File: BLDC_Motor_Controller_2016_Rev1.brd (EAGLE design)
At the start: 113.7 x 80 mm, 98 parts, among them Q1 MOSFET-NCHANNELFQP30N06L, Q2 MOSFET-NCHANNELFQP30N06L, Q3 MOSFET-NCHANNELFQP30N06L, Q4 MOSFET-NCHANNELFQP30N06L, Q5 MOSFET-NCHANNELFQP30N06L, Q6 MOSFET-NCHANNELFQP30N06L, Q7 MOSFET-PCHANNEL, Q8 MOSFET-PCHANNEL

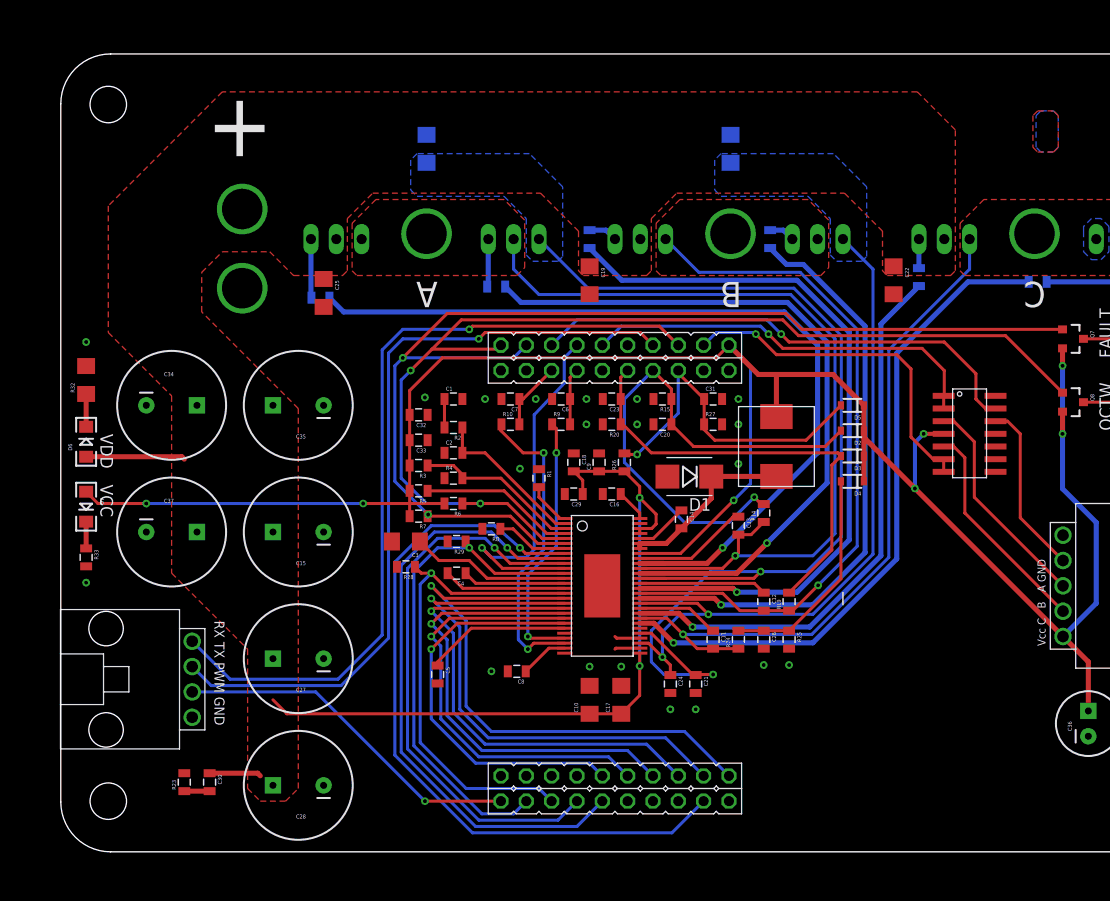
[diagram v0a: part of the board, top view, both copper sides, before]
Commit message: Swapped SL connectors, added APP spacer
Swapped 4-pin Molex SL for two 3-pin SL connectors, added mounting wing
between power inputs, added board description and MRDT logo, moved big
caps around
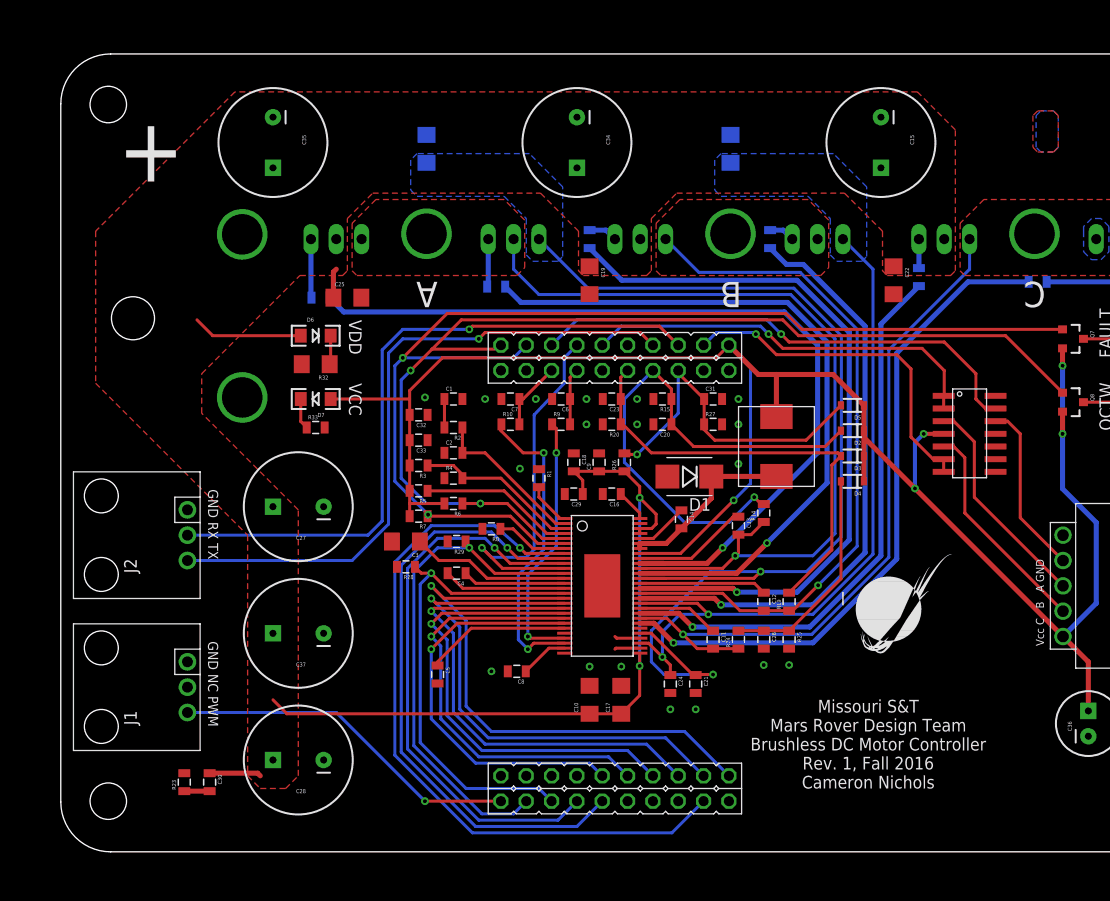
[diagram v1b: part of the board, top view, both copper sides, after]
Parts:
- added J1, J2: SL03THROUGH_HOLE, MRDT-Connectors:MOLEX_SL_03_THROUGH_HOLE
- added U$10: APP_MOUTING_WINGHORIZ, MRDT-Connectors:APP45_MOUNTING_WING_HORIZ
- U$9: value 4PIN -> (none); device Molex-SL:4PIN -> MRDT-Hardware:MRDT_LOGO
- moved C15 70.3 mm to (78.7, 69.8), turned to 270 degrees
- moved U$9 66.5 mm to (76.2, 17.8), turned to 0 degrees
- moved C34 48.4 mm to (48.3, 69.8), turned to 270 degrees
- moved C35 26.5 mm to (17.8, 69.8), turned to 270 degrees
- moved R33 26.4 mm to (22.1, 41.3), turned to 0 degrees
- moved D7 25.4 mm to (22.1, 44.1), turned to 180 degrees
- moved D6 25.4 mm to (22.1, 50.5), turned to 0 degrees
- moved R32 23.1 mm to (22.1, 47.6), turned to 180 degrees
- moved C37 16.3 mm to (20.3, 20.6), turned to 180 degrees
- moved C27 15.2 mm to (20.3, 33.3)
- moved U$4 11.0 mm to (-13.5, 40.3)
- moved C28 2.54 mm to (20.3, 7.94)
- moved U$3 2.54 mm to (-13.5, 56.7)
- moved C25 2.43 mm to (25.2, 54.3), turned to 0 degrees
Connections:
- new net N$36: J1.2
- net GND: now also J1.1, J2.1; no longer U$9.4
- net RX: now also J2.2; no longer U$9.1
- net SPEED_IN: now also J1.3; no longer U$9.3
- net TX: now also J2.3; no longer U$9.2
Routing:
- net VCC: track 218.8 -> 193.8 mm, vias 7 -> 5
- net RX: track 82.5 -> 68.7 mm
- net TX: track 78.9 -> 66.7 mm
- net PVDD: track 91.1 -> 95.2 mm
- net GND: vias 22 -> 20
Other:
- board text added: "GND NC PWM"
- board text added: "GND RX TX"
- board text added: "Missouri S&T Mars Rover Design Team Brushless DC Motor Controller Rev. 1, Fall 2016 Cameron Nichols"
- board text removed: "RX TX PWM GND"

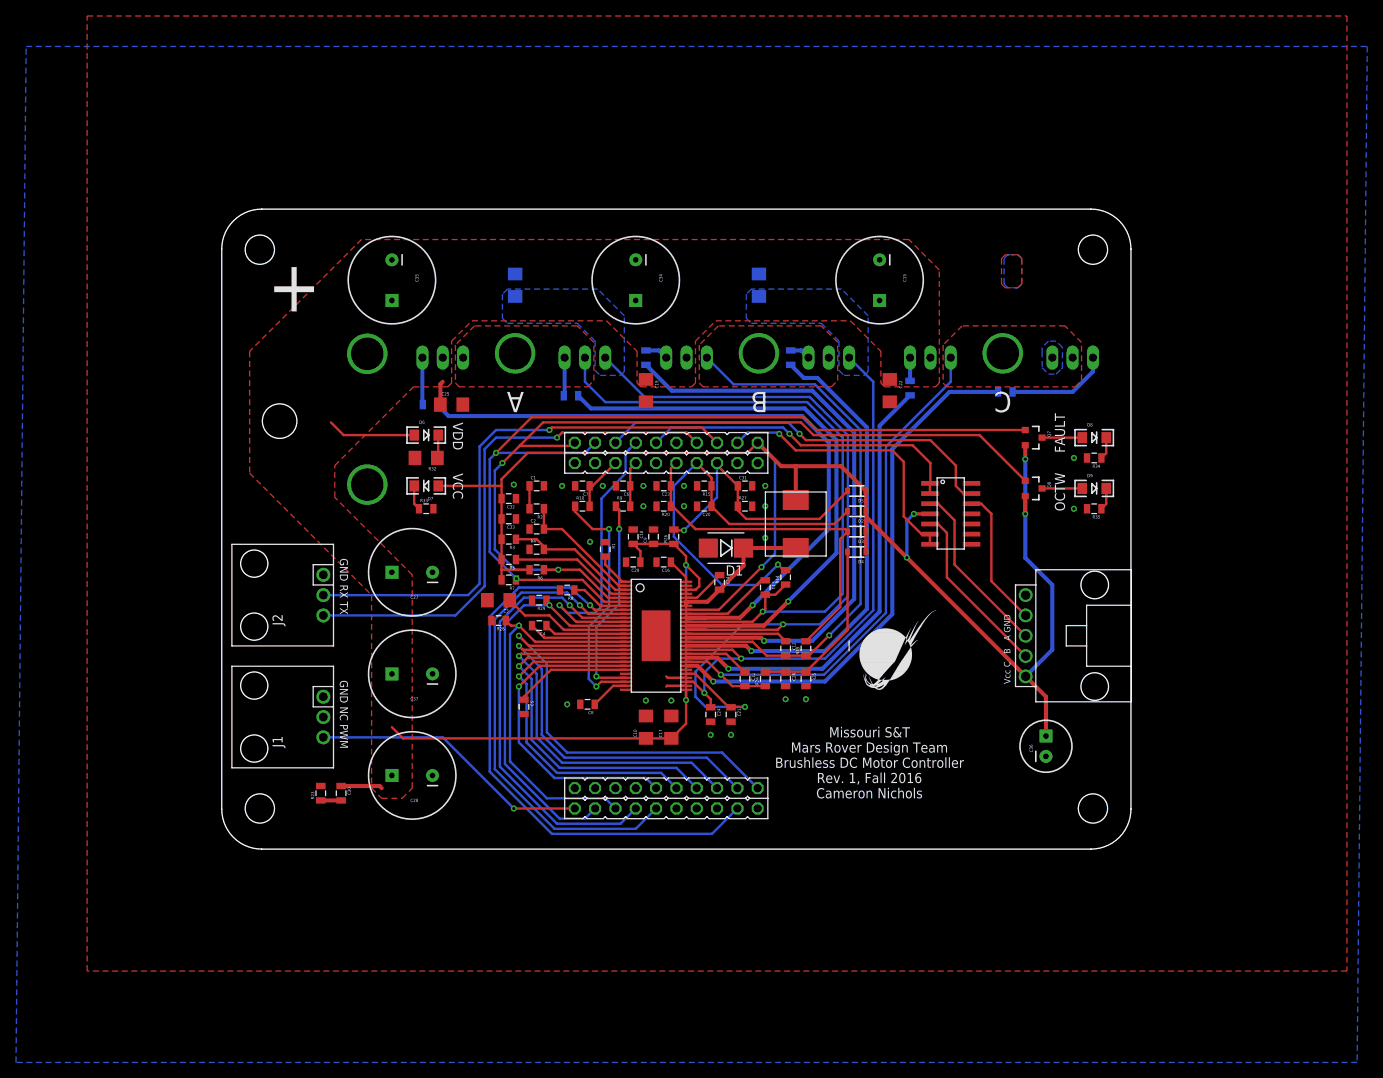
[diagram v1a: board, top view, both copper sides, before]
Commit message: Swapped side-by-side anderson input with stacked orientation
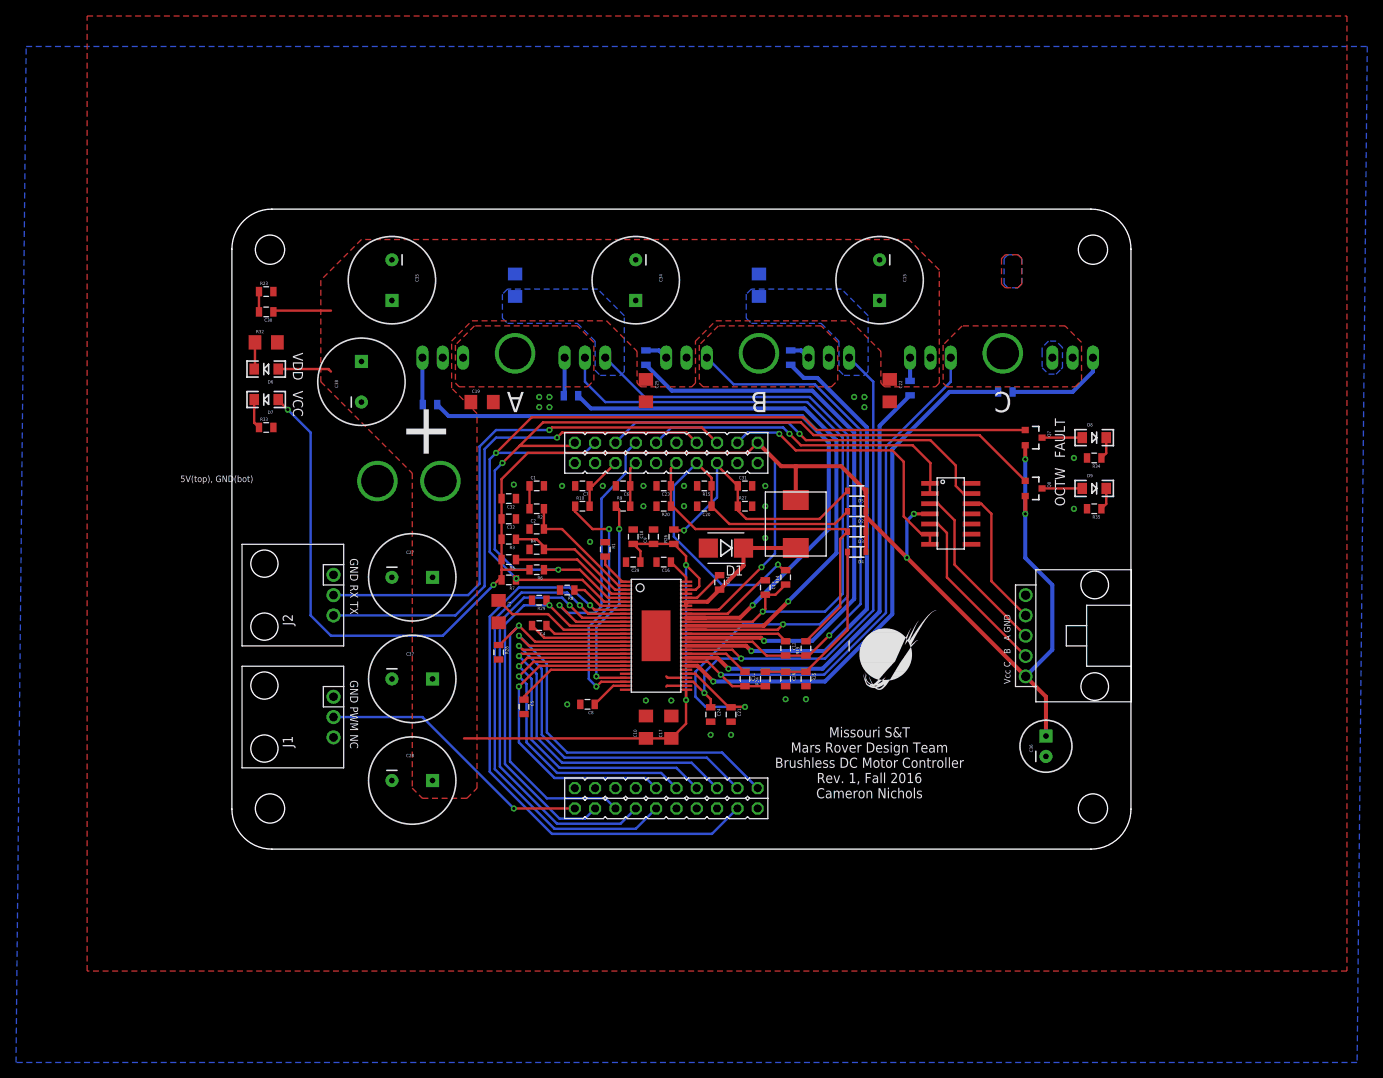
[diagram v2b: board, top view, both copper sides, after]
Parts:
- removed U$10: APP_MOUTING_WINGHORIZ, MRDT-Connectors:APP45_MOUNTING_WING_HORIZ
- removed U$3, U$4: APPPP45_PCB_HORIZ_RIGHT, MRDT-Connectors:APP45_PCB_HORIZ_RIGHT
- added C38: 220u, SparkFun-Passives:CPOL-RADIAL-1000UF-25V
- added J3: APP_2POS_CONFIG5V_HORIZ, MRDT-Connectors:APP45_5V_HORIZ_CONFIG
- J1: value SL03THROUGH_HOLE -> SERVOMOLEX_SL_THRU_HOLE
- moved R23 63.1 mm to (2.06, 68.4), turned to 0 degrees
- moved C30 60.9 mm to (2.06, 65.9), turned to 180 degrees
- moved R32 24.7 mm to (2.06, 62.1), turned to 0 degrees
- moved C25 24.4 mm to (49.5, 56.0), turned to 270 degrees
- moved D7 22.7 mm to (2.06, 54.9)
- moved R33 22.4 mm to (2.06, 51.4)
- moved D6 21.6 mm to (2.06, 58.7), turned to 180 degrees
- moved C19 20.5 mm to (29.1, 54.6), turned to 0 degrees
- moved R28 3.97 mm to (31.1, 23.3), turned to 270 degrees
- moved C3 1.43 mm to (31.1, 28.4), turned to 270 degrees
- moved J1 1.27 mm to (10.5, 15.2)
- moved J2 1.27 mm to (10.5, 30.5)
- moved C28 0.63 mm to (20.3, 7.30), turned to 0 degrees
- moved C27 0.63 mm to (20.3, 32.7), turned to 0 degrees
- moved C37 0.63 mm to (20.3, 20.0), turned to 0 degrees
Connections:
- removed net N$36: J1.2
- net GND: now also C38.2, J3.GND; no longer U$4.P$1
- net PVDD: now also C38.1, J3.5V; no longer U$3.P$1
- net SPEED_IN: now also J1.2; no longer J1.3
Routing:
- net VCC: track 193.8 -> 242.5 mm, vias 5 -> 7
- net PVDD: track 95.2 -> 80.3 mm
- net EN_GATE: track 49.2 -> 50.8 mm
- net N$8: track 16.1 -> 17.5 mm
- net TX: track 66.7 -> 65.4 mm
- net RX: track 68.7 -> 67.5 mm
- net N$24: track 3.11 -> 3.74 mm
- net GND: vias 20 -> 27
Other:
- board size 113.7 x 80 mm -> 112.4 x 80 mm
- board text added: "GND PWM NC"
- board text removed: "GND NC PWM"

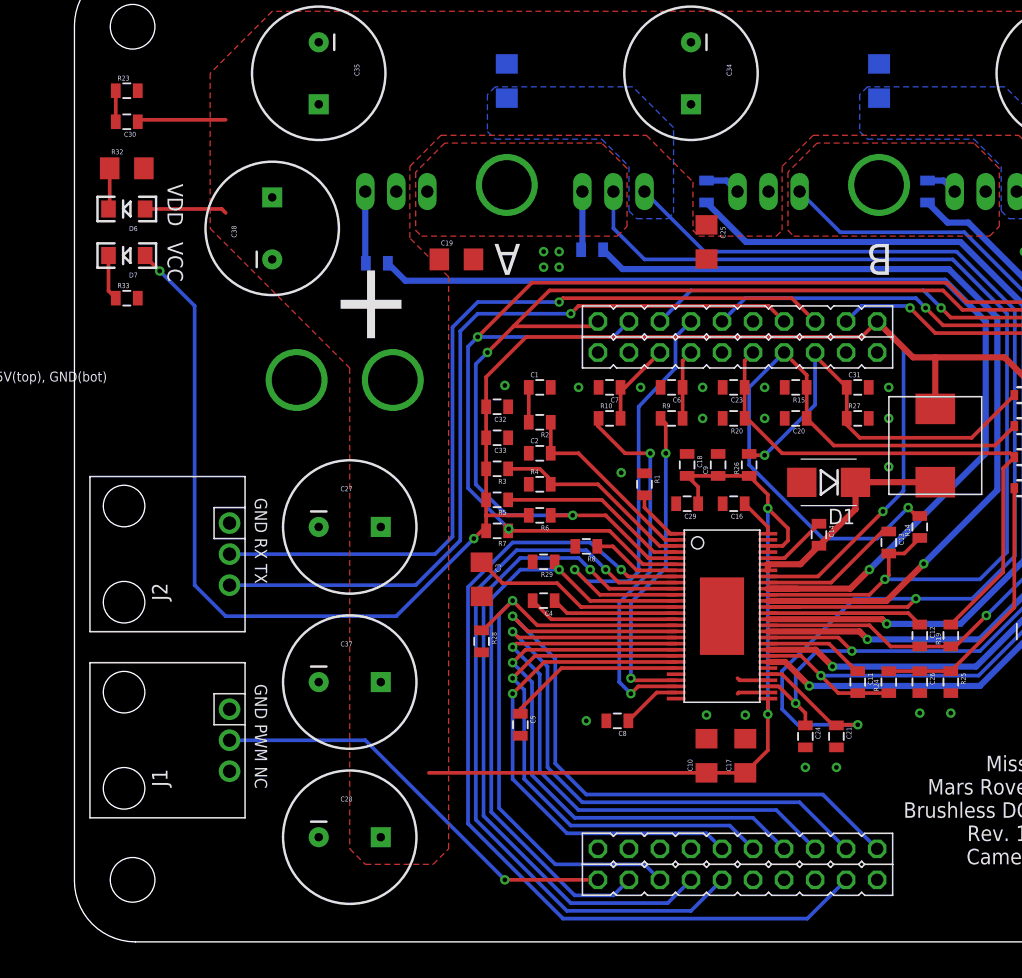
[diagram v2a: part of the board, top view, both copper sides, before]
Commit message: Added RS-485 IC to replace UART
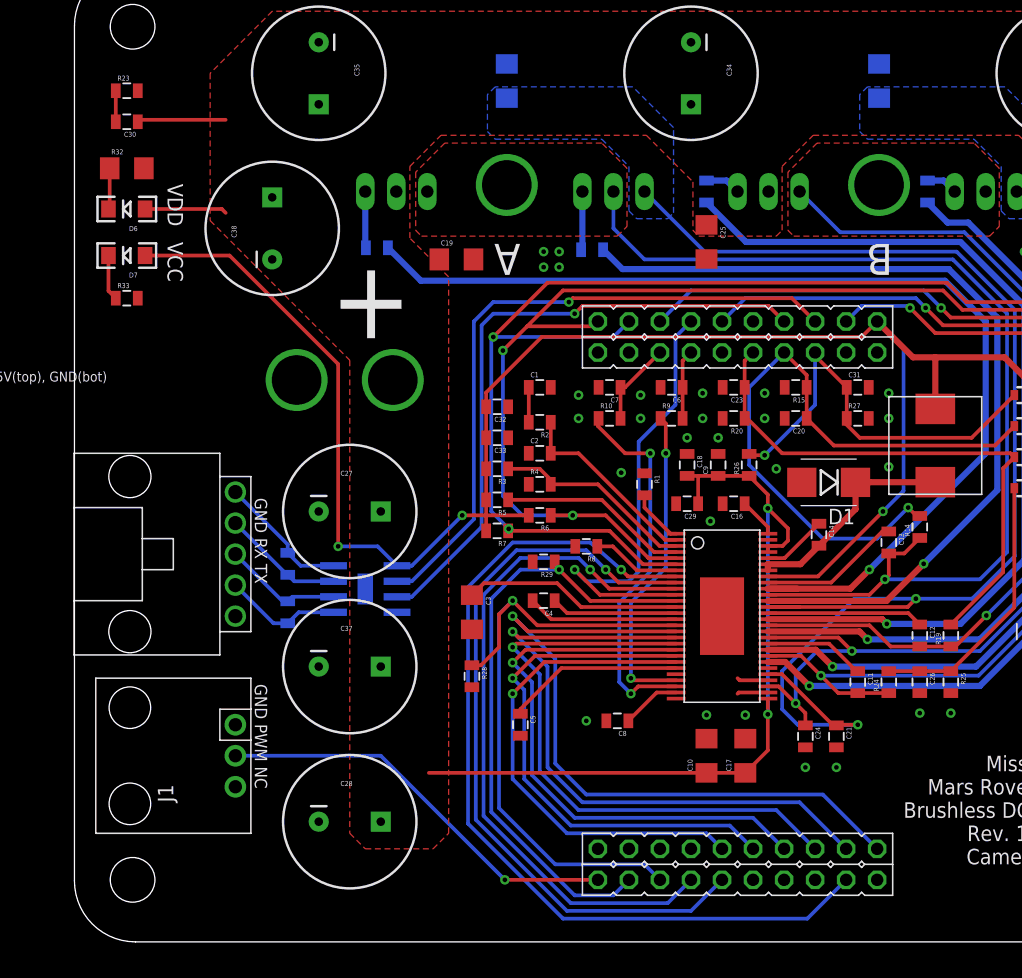
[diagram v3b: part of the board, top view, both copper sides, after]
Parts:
- removed J2: SL03THROUGH_HOLE, MRDT-Connectors:MOLEX_SL_03_THROUGH_HOLE
- added R30, R31: 3.3, SparkFun-Passives:0805
- added U$3: MAX3077, MRDT-2015-General:SO8
- added U$4: 5PIN, Molex-SL:5PIN
- moved R28 2.97 mm to (30.3, 20.5)
- moved C3 2.81 mm to (30.3, 25.7)
- moved J1 1.36 mm to (11.0, 14.0)
- moved R11 1.27 mm to (22.5, 55.6)
- moved C28 1.27 mm to (20.3, 8.57)
- moved C37 1.27 mm to (20.3, 21.3)
- moved C27 1.27 mm to (20.3, 34.0)
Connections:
- new net N$34: R30.2, U$3.5, U$4.4
- new net N$36: R30.1, U$3.6, U$4.3
- new net N$37: R31.2, U$3.7, U$4.2
- new net N$38: R31.1, U$3.8, U$4.1
- net GND: now also U$3.4, U$4.5; no longer J2.1
- net RX: now also U$3.2; no longer J2.2
- net TX: now also U$3.3; no longer J2.3
- net VCC: now also U$3.1
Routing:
- net TX: track 65.4 -> 51.8 mm
- net RX: track 67.5 -> 54.1 mm
- net N$38: track 0.00 -> 10.9 mm
- net N$37: track 0.00 -> 10.0 mm
- net N$36: track 0.00 -> 9.79 mm
- net N$34: track 0.00 -> 9.70 mm
- net VCC: track 242.5 -> 234.0 mm
- net NOCTW: track 109.5 -> 105.1 mm
- net NFAULT: track 114.1 -> 110.5 mm
- net EN_GATE: track 50.8 -> 54.4 mm
- net N$13: track 5.90 -> 4.63 mm
- net SPEED_IN: track 34.9 -> 33.9 mm
- net GH_A: track 86.6 -> 87.1 mm
- net GND: vias 27 -> 32
